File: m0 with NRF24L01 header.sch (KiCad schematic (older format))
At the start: 24 parts, among them J1 UART, J10 Conn_01x05_Female Taranis I/O, J12 Batt Conn, J13 SPI, J2 I2C, J3 Extra Pins, J4 Extra Pins GND, J5 Extra Pins 3V3, J6 ARDU_PINS, J7 ARDU_PINS_GND, J8 ARDU_PINS_3V3, J9 NRF24L01 Module, Q1 SI2304DDS-T1-GE3, Q2 SI2304DDS-T1-GE3, U2 NCP1117ST33T3G

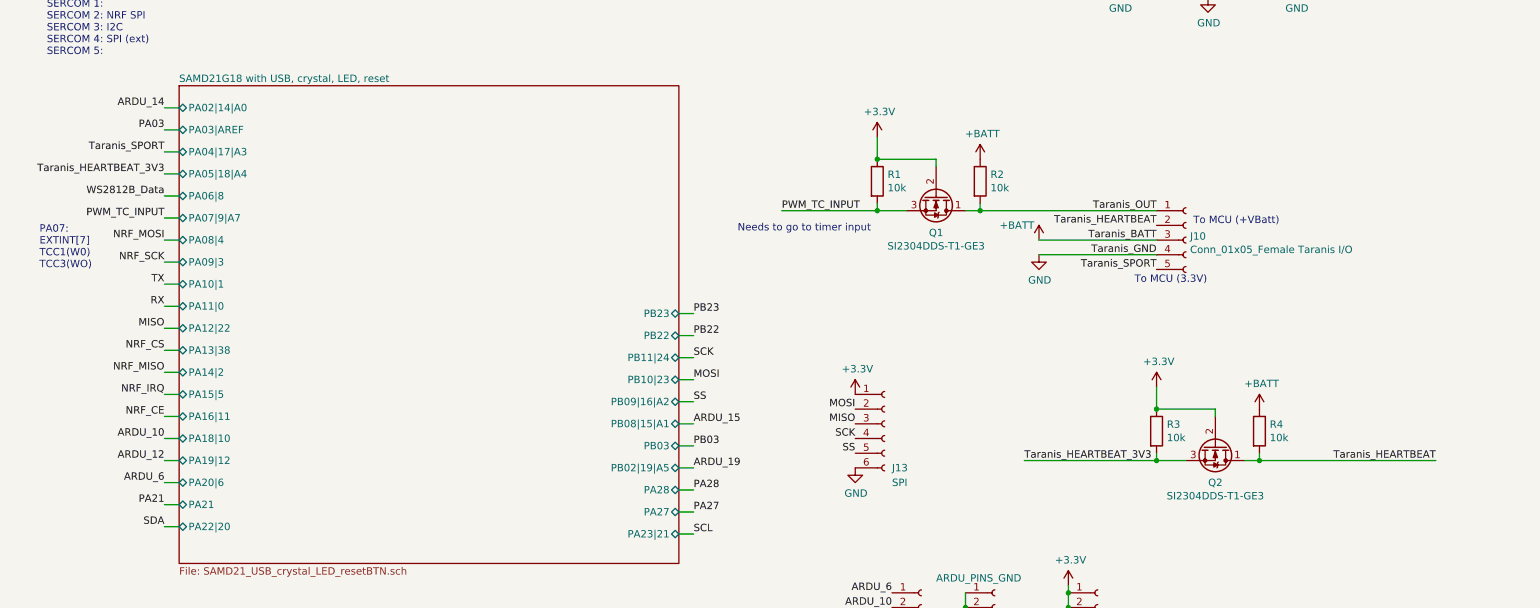
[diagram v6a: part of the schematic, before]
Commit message: Remove Taranis level conversion
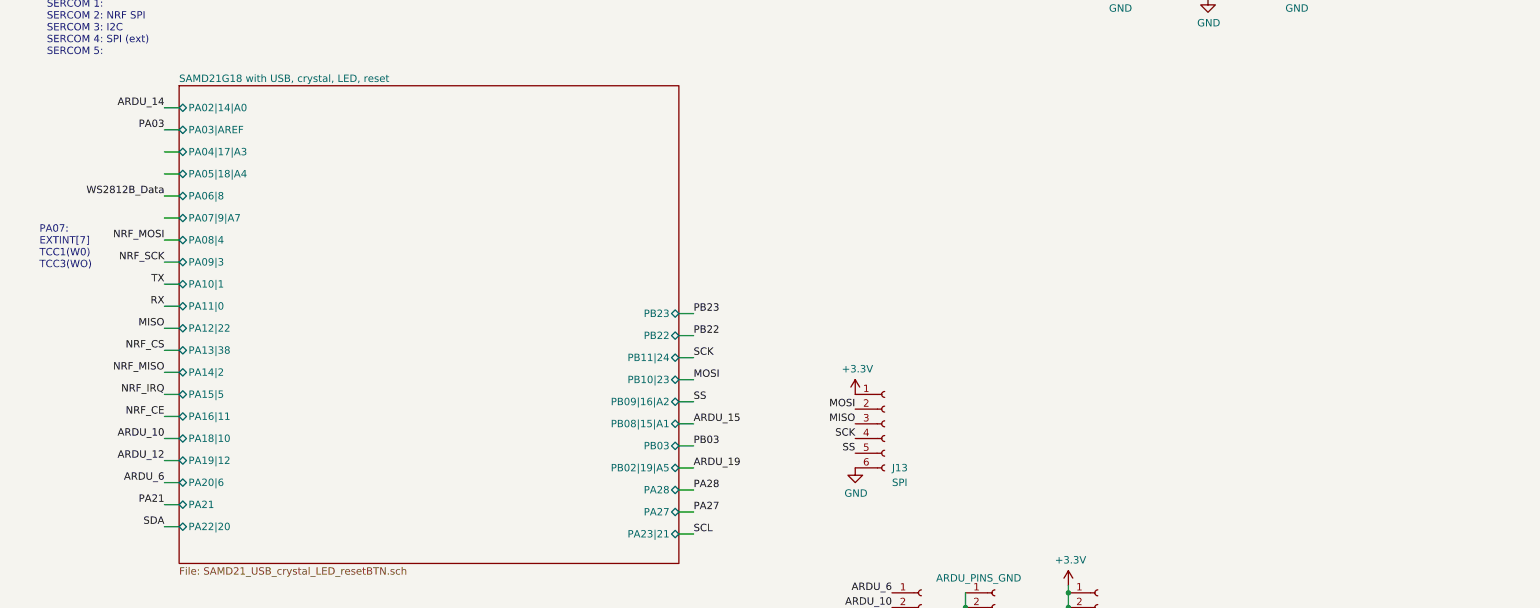
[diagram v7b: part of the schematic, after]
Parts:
- removed J10: Conn_01x05_Female Taranis I/O, Connector_PinHeader_2.54mm:PinHeader_1x05_P2.54mm_Vertical, symbol Connector:Conn_01x05_Female
- removed Q1, Q2: SI2304DDS-T1-GE3, Package_TO_SOT_SMD:SOT-23, symbol Device:Q_NMOS_DGS
- removed R1, R2, R3, R4: 10k, Resistor_SMD:R_0603_1608Metric, symbol Device:R
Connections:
- net labels removed: PWM_TC_INPUT, Taranis_BATT, Taranis_GND, Taranis_HEARTBEAT, Taranis_HEARTBEAT_3V3, Taranis_OUT, Taranis_SPORT
- wire segments 92 -> 72
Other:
- note removed: "Needs to go to timer input"
- note removed: "To MCU (+VBatt)"
- note removed: "To MCU (3.3V)"
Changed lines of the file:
@@
 	1    0    0    -1
 $EndComp
-$Comp
-L Connector:Conn_01x05_Female J10
-U 1 1 5C323AEA
-P 8350 3050
-F 0 "J10" H 8378 3076 50  0000 L CNN
-F 1 "Conn_01x05_Female Taranis I/O" H 8378 2985 50  0000 L CNN
-F 2 "Connector_PinHeader_2.54mm:PinHeader_1x05_P2.54mm_Vertical" H 8350 3050 50  0001 C CNN
-F 3 "~" H 8350 3050 50  0001 C CNN
-	1    8350 3050
-	1    0    0    -1
-$EndComp
-Text Label 8150 2850 2    50   ~ 0
-Taranis_OUT
-Text Label 8150 2950 2    50   ~ 0
-Taranis_HEARTBEAT
-Text Label 8150 3050 2    50   ~ 0
-Taranis_BATT
-Text Label 8150 3150 2    50   ~ 0
-Taranis_GND
-Text Label 8150 3250 2    50   ~ 0
-Taranis_SPORT
 Text Label 4050 900  2    50   ~ 0
 NRF_GND
@@
 Text Label 4550 1200 0    50   ~ 0
 NRF_IRQ
-$Comp
-L Device:Q_NMOS_DGS Q1
-U 1 1 5C3240E7
-P 6650 2750
-F 0 "Q1" V 6900 2750 50  0000 C CNN
-F 1 "SI2304DDS-T1-GE3" V 6991 2750 50  0000 C CNN
-F 2 "Package_TO_SOT_SMD:SOT-23" H 6850 2850 50  0001 C CNN
-F 3 "~" H 6650 2750 50  0001 C CNN
-	1    6650 2750
-	0    1    1    0
-$EndComp
-Wire Wire Line
-	8150 2850 6950 2850
-$Comp
-L power:+BATT #PWR0110
-U 1 1 5C32425E
-P 7350 3050
-F 0 "#PWR0110" H 7350 2900 50  0001 C CNN
-F 1 "+BATT" H 7200 3150 50  0000 C CNN
-F 2 "" H 7350 3050 50  0001 C CNN
-F 3 "" H 7350 3050 50  0001 C CNN
-	1    7350 3050
-	1    0    0    -1
-$EndComp
-Wire Wire Line
-	7350 3050 8150 3050
-$Comp
-L power:GND #PWR0112
-U 1 1 5C3242E4
-P 7350 3150
-F 0 "#PWR0112" H 7350 2900 50  0001 C CNN
-F 1 "GND" H 7355 2977 50  0000 C CNN
-F 2 "" H 7350 3150 50  0001 C CNN
-F 3 "" H 7350 3150 50  0001 C CNN
-	1    7350 3150
-	1    0    0    -1
-$EndComp
-$Comp
-L Device:R R2
-U 1 1 5C32433C
-P 6950 2650
-F 0 "R2" H 7020 2696 50  0000 L CNN
-F 1 "10k" H 7020 2605 50  0000 L CNN
-F 2 "Resistor_SMD:R_0603_1608Metric" V 6880 2650 50  0001 C CNN
-F 3 "~" H 6950 2650 50  0001 C CNN
-	1    6950 2650
-	1    0    0    -1
-$EndComp
-$Comp
-L Device:R R1
-U 1 1 5C324454
-P 6250 2650
-F 0 "R1" H 6320 2696 50  0000 L CNN
-F 1 "10k" H 6320 2605 50  0000 L CNN
-F 2 "Resistor_SMD:R_0603_1608Metric" V 6180 2650 50  0001 C CNN
-F 3 "~" H 6250 2650 50  0001 C CNN
-	1    6250 2650
-	1    0    0    -1
-$EndComp
-$Comp
-L power:+3.3V #PWR0113
-U 1 1 5C3244A1
-P 6250 2350
-F 0 "#PWR0113" H 6250 2200 50  0001 C CNN
-F 1 "+3.3V" H 6265 2523 50  0000 C CNN
-F 2 "" H 6250 2350 50  0001 C CNN
-F 3 "" H 6250 2350 50  0001 C CNN
-	1    6250 2350
-	1    0    0    -1
-$EndComp
-Wire Wire Line
-	6250 2350 6250 2500
-Wire Wire Line
-	6250 2500 6650 2500
-Wire Wire Line
-	6650 2500 6650 2550
-Connection ~ 6250 2500
-Wire Wire Line
-	6450 2850 6250 2850
-Wire Wire Line
-	6250 2850 6250 2800
-Wire Wire Line
-	6950 2800 6950 2850
-Connection ~ 6950 2850
-Wire Wire Line
-	6950 2850 6850 2850
-Connection ~ 6250 2850
-$Comp
-L power:+BATT #PWR0114
-U 1 1 5C324707
-P 6950 2500
-F 0 "#PWR0114" H 6950 2350 50  0001 C CNN
-F 1 "+BATT" H 6965 2673 50  0000 C CNN
-F 2 "" H 6950 2500 50  0001 C CNN
-F 3 "" H 6950 2500 50  0001 C CNN
-	1    6950 2500
-	1    0    0    -1
-$EndComp
 Text Label 1400 3200 2    50   ~ 0
 NRF_SCK
@@
 Wire Wire Line
 	1400 4250 1500 4250
-Text Notes 5300 3000 0    50   ~ 0
-Needs to go to timer input
-Text Notes 8000 3350 0    50   ~ 0
-To MCU (3.3V)
-Text Notes 8400 2950 0    50   ~ 0
-To MCU (+VBatt)
-Wire Wire Line
-	7350 3150 8150 3150
 Text Label 1650 900  2    50   ~ 0
 TX
@@
 Text Label 2750 1050 2    50   ~ 0
 SDA
-Text Label 5600 2850 0    50   ~ 0
-PWM_TC_INPUT
-Wire Wire Line
-	5600 2850 6250 2850
-Text Label 1400 2900 2    50   ~ 0
-PWM_TC_INPUT
 Wire Wire Line
 	1400 2900 1500 2900
 Text Notes 550  3250 0    50   ~ 0
 PA07:\nEXTINT[7]\nTCC1(W0)\nTCC3(WO)
-$Comp
-L Device:Q_NMOS_DGS Q2
-U 1 1 5C3A71AE
-P 8550 4450
-F 0 "Q2" V 8800 4450 50  0000 C CNN
-F 1 "SI2304DDS-T1-GE3" V 8891 4450 50  0000 C CNN
-F 2 "Package_TO_SOT_SMD:SOT-23" H 8750 4550 50  0001 C CNN
-F 3 "~" H 8550 4450 50  0001 C CNN
-	1    8550 4450
-	0    1    1    0
-$EndComp
-Wire Wire Line
-	10050 4550 8850 4550
-$Comp
-L Device:R R4
-U 1 1 5C3A71B6
-P 8850 4350
-F 0 "R4" H 8920 4396 50  0000 L CNN
-F 1 "10k" H 8920 4305 50  0000 L CNN
-F 2 "Resistor_SMD:R_0603_1608Metric" V 8780 4350 50  0001 C CNN
-F 3 "~" H 8850 4350 50  0001 C CNN
-	1    8850 4350
-	1    0    0    -1
-$EndComp
-$Comp
-L Device:R R3
-U 1 1 5C3A71BD
-P 8150 4350
-F 0 "R3" H 8220 4396 50  0000 L CNN
-F 1 "10k" H 8220 4305 50  0000 L CNN
-F 2 "Resistor_SMD:R_0603_1608Metric" V 8080 4350 50  0001 C CNN
-F 3 "~" H 8150 4350 50  0001 C CNN
-	1    8150 4350
-	1    0    0    -1
-$EndComp
-$Comp
-L power:+3.3V #PWR0122
-U 1 1 5C3A71C4
-P 8150 4050
-F 0 "#PWR0122" H 8150 3900 50  0001 C CNN
-F 1 "+3.3V" H 8165 4223 50  0000 C CNN
-F 2 "" H 8150 4050 50  0001 C CNN
-F 3 "" H 8150 4050 50  0001 C CNN
-	1    8150 4050
-	1    0    0    -1
-$EndComp
-Wire Wire Line
-	8150 4050 8150 4200
-Wire Wire Line
-	8150 4200 8550 4200
-Wire Wire Line
-	8550 4200 8550 4250
-Connection ~ 8150 4200
-Wire Wire Line
-	8350 4550 8150 4550
-Wire Wire Line
-	8150 4550 8150 4500
-Wire Wire Line
-	8850 4500 8850 4550
-Connection ~ 8850 4550
-Wire Wire Line
-	8850 4550 8750 4550
-Connection ~ 8150 4550
-$Comp
-L power:+BATT #PWR0123
-U 1 1 5C3A71D4
-P 8850 4200
-F 0 "#PWR0123" H 8850 4050 50  0001 C CNN
-F 1 "+BATT" H 8865 4373 50  0000 C CNN
-F 2 "" H 8850 4200 50  0001 C CNN
-F 3 "" H 8850 4200 50  0001 C CNN
-	1    8850 4200
-	1    0    0    -1
-$EndComp
-Text Label 7250 4550 0    50   ~ 0
-Taranis_HEARTBEAT_3V3
-Wire Wire Line
-	7250 4550 8150 4550
-Text Label 10050 4550 2    50   ~ 0
-Taranis_HEARTBEAT
-Text Label 1400 2600 2    50   ~ 0
-Taranis_HEARTBEAT_3V3
 Wire Wire Line
 	1400 2600 1500 2600
-Text Label 1400 2450 2    50   ~ 0
-Taranis_SPORT
 Wire Wire Line
 	1400 2450 1500 2450

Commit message: Replace header with 0.1" and 0805 capacitor
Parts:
- J12: footprint Connector_PinHeader_1.27mm:PinHeader_1x02_P1.27mm_Vertical -> Connector_PinHeader_2.54mm:PinHeader_1x02_P2.54mm_Vertical
- J13: footprint Connector_PinHeader_1.27mm:PinHeader_1x06_P1.27mm_Vertical -> Connector_PinHeader_2.54mm:PinHeader_1x06_P2.54mm_Vertical
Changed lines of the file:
@@
 F 0 "J12" H 6600 1050 50  0000 C CNN
 F 1 "Batt Conn" H 6600 900 50  0000 C CNN
-F 2 "Connector_PinHeader_1.27mm:PinHeader_1x02_P1.27mm_Vertical" H 6500 1100 50  0001 C CNN
+F 2 "Connector_PinHeader_2.54mm:PinHeader_1x02_P2.54mm_Vertical" H 6500 1100 50  0001 C CNN
 F 3 "~" H 6500 1100 50  0001 C CNN
 	1    6500 1100
@@
 F 0 "J13" H 6350 4000 50  0000 L CNN
 F 1 "SPI" H 6350 3900 50  0000 L CNN
-F 2 "Connector_PinHeader_1.27mm:PinHeader_1x06_P1.27mm_Vertical" H 6300 4300 50  0001 C CNN
+F 2 "Connector_PinHeader_2.54mm:PinHeader_1x06_P2.54mm_Vertical" H 6300 4300 50  0001 C CNN
 F 3 "~" H 6300 4300 50  0001 C CNN
 	1    6300 4300
